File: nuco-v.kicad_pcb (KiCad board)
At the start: 2 copper layers, 70 x 82.5 mm, 141 parts, among them Q1 1N7002, Q2 1N7002, Q3 NTS4173, Q4 NTS4173, SW1 BUTTON1, SW2 BUTTON1, SW3 BUTTON1, U1 STM32H742Vx, U10 LP2985N, U2 LM1117, U3 LD39050PU, U4 SN74LVC2T45, U5 SN74LVC2T45, U6 SN74LVC2T45, U7 SN74LVC2T45, U8 ESDA5V3SC6, U9 STM32F103CBT6, X1 ST-MORPHO-CN7, X10 CONN-12P2L, X11 CONN-10P2L, X12 CONN-02P1LA, X13 CONN-02P1LA, X14 CONN-06P1L, X15 CONN-02P1L, X2 CONN-08P1L, X3 CONN-06P1L, X4 CONN-03P1L, X5 CONN-10P1L, X6 CONN-08P1L, X7 ST-MORPHO-CN10, X8 USB-OTG, X9 CONN-04P1L, Y1 32.768K, Y2 8MHz, Y3 8MHz

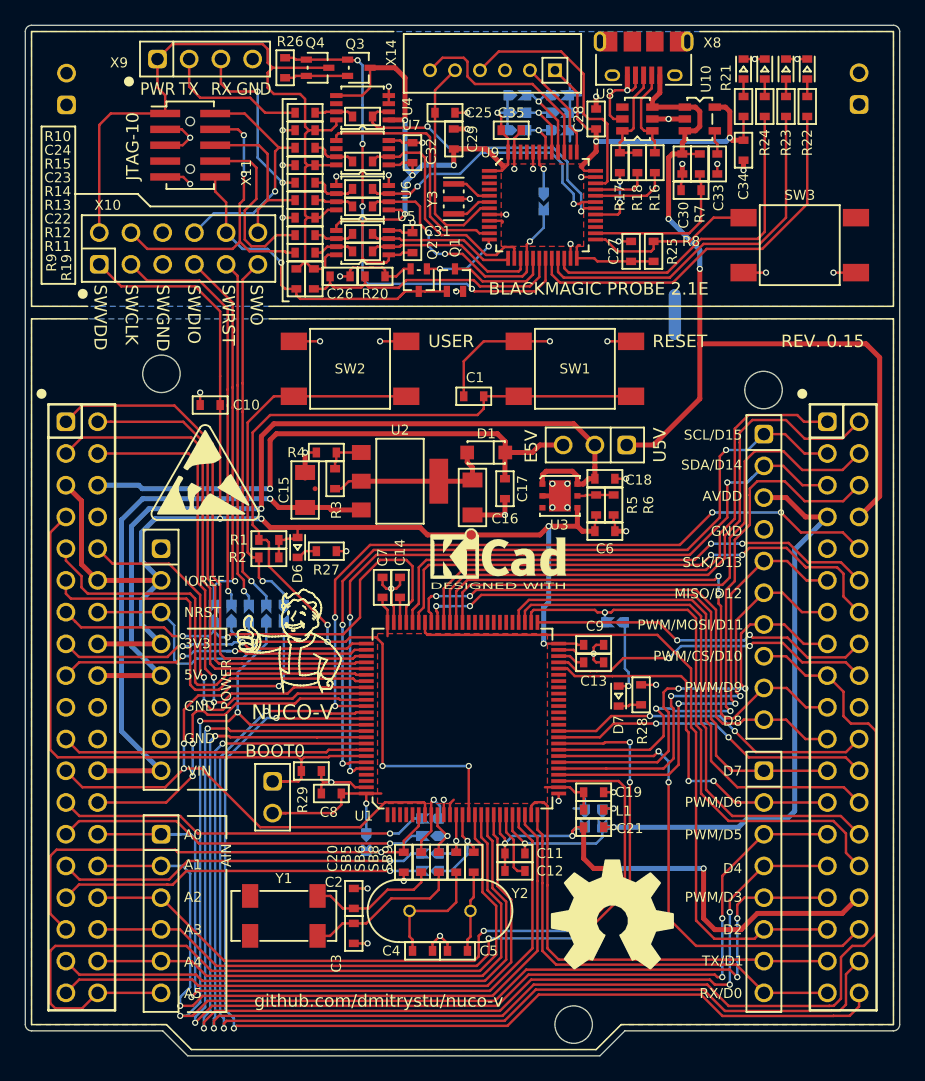
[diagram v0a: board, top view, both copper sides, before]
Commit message: Updated to KiCad V8
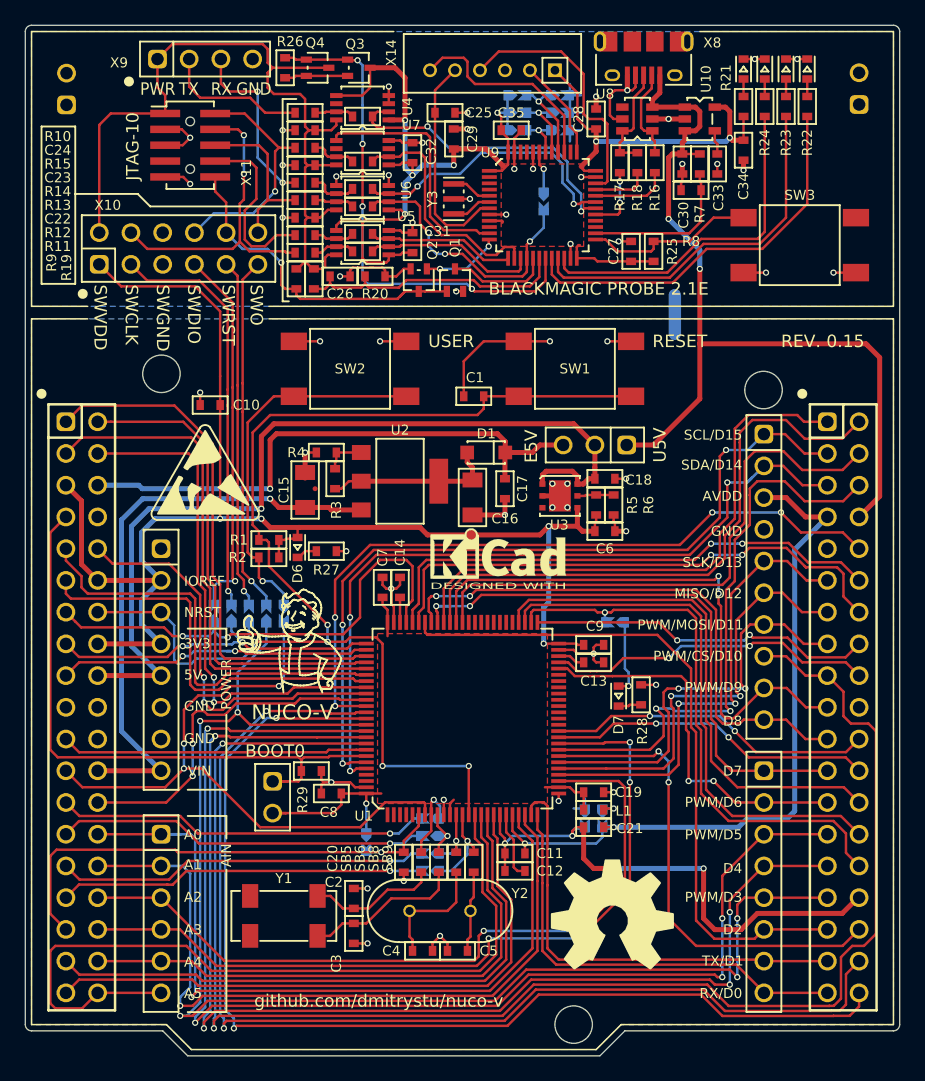
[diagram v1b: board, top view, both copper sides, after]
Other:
- net class Default removed
- net class PWR removed
